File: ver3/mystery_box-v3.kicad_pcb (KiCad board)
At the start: 2 copper layers, 136 x 100 mm, 58 parts, among them J1 Screw_Terminal_01x02, J10 Screw_Terminal_01x02, J11 Screw_Terminal_01x02, J12 Screw_Terminal_01x02, J13 Screw_Terminal_01x02, J14 Screw_Terminal_01x02, J15 Screw_Terminal_01x02, J16 Screw_Terminal_01x02, J17 Screw_Terminal_01x02, J18 Barrel_Jack_MountingPin, J2 XLR3, J20 rj45-CC-X2-Aliexpress, J8 Screw_Terminal_01x02, J9 Screw_Terminal_01x02, M1 24V-Boost-Converter, Q1 IRLZ44N, Q2 IRLZ44N, Q3 IRLZ44N, U1 THVD1400D

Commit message: logo + silk stuff
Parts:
- added 12V_FAN: Conn_01x02_Pin, Connector_PinHeader_2.54mm:PinHeader_1x02_P2.54mm_Vertical, F.Cu at (259.1, 72.3)
- U3: value ~ -> smart switch
- renumbered GREEN1 to PWR_LED, switched_output_01 to SW_01, switched_output_02 to SW_02, switched_output_03 to SW_03
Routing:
- net VCC 12V: track 191.7 -> 203.5 mm
- net VCC 5V USB: track 88.4 -> 78.6 mm
- net Net-(U3-IN): track 57.9 -> 62.2 mm
- net Net-(U3-ST): track 55.8 -> 59.3 mm
- net GND: track 0.00 -> 2.87 mm, vias 1 -> 28
- net VCC 12V SW: track 356.7 -> 356.1 mm
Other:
- board text added: "+ -"
- board text added: "- d +"
- board text added: "12V always ON"
- board text added: "12V always ON fused"
- board text added: "Cosmic Cable Ltd. Mystery Box Pro"
- board text added: "RX"
- board text added: "TX"
- board text added: "rev. 1"
- board text added: "v3"

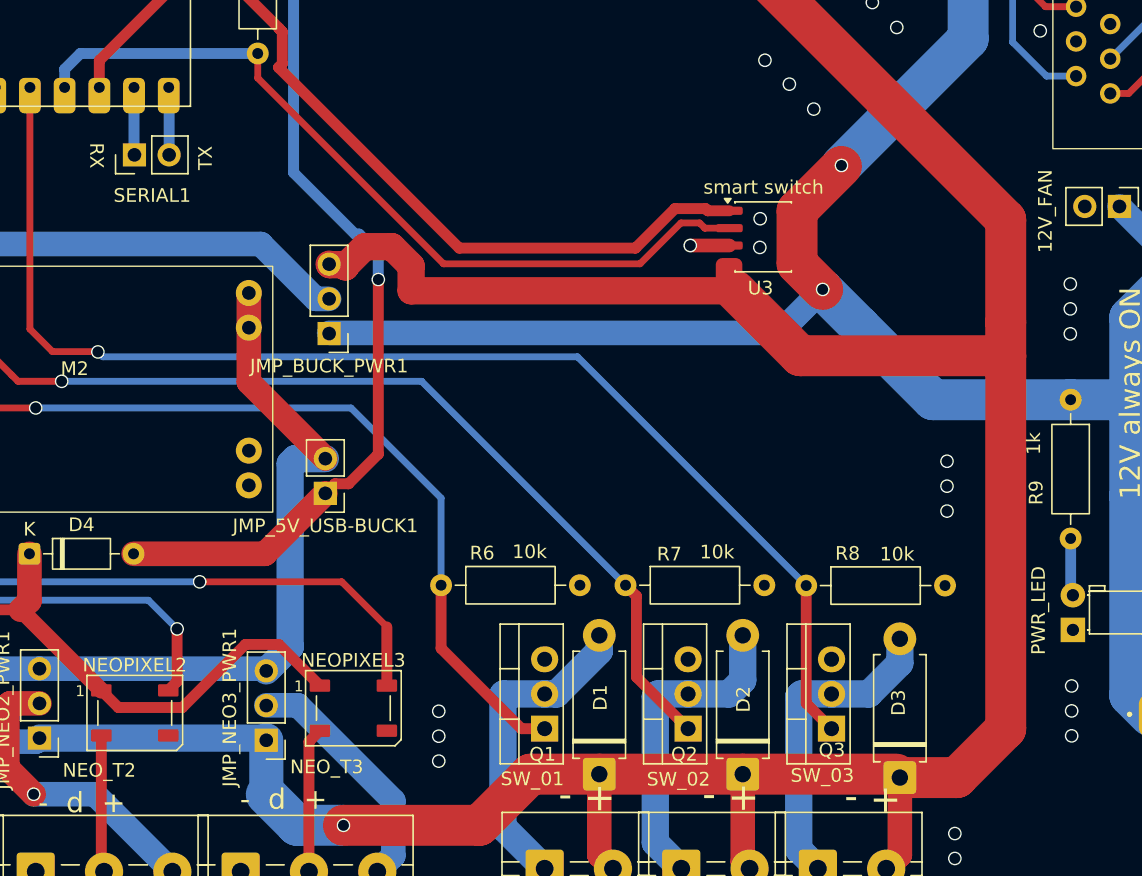
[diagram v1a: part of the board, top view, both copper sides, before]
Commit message: ver3: added GND to serial1
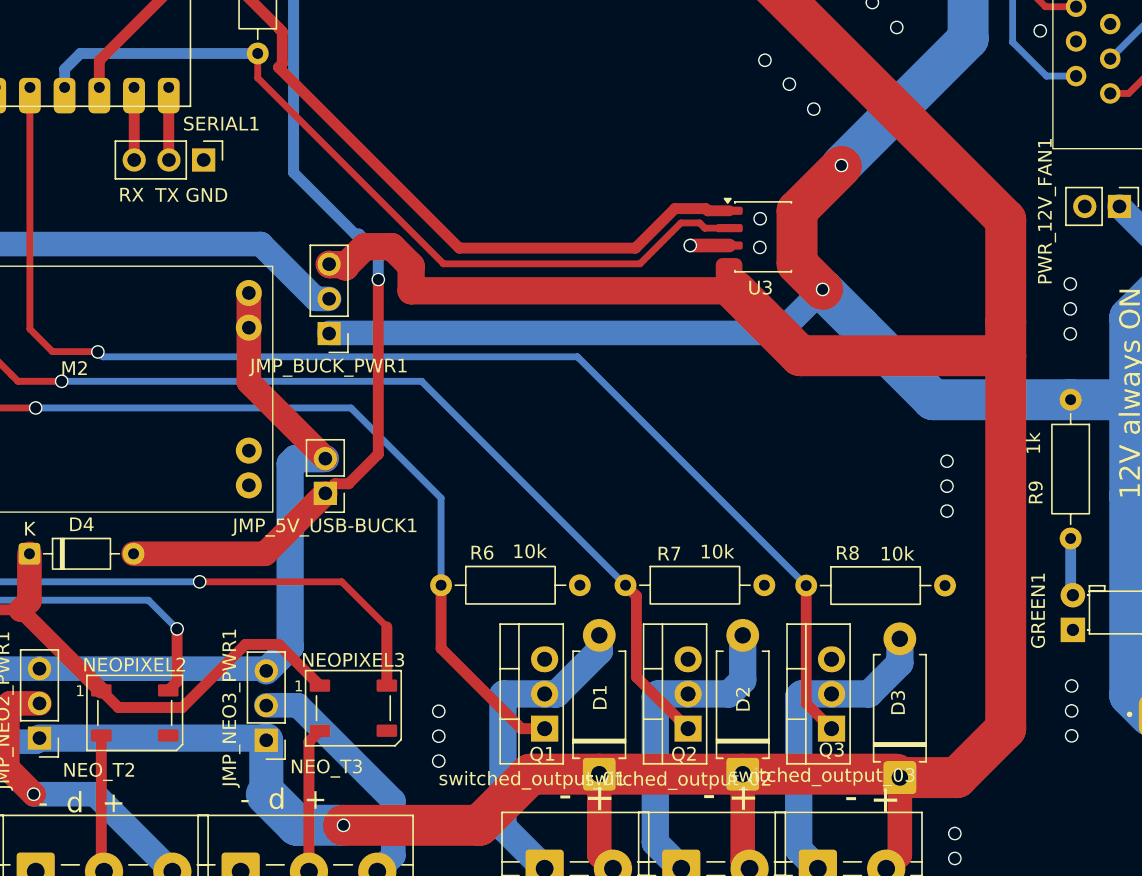
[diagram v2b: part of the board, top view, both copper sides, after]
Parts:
- removed SERIAL1: Conn_01x02_Pin, Connector_PinHeader_2.54mm:PinHeader_1x02_P2.54mm_Vertical
- added J3: SERIAL1, Connector_PinHeader_2.54mm:PinHeader_1x03_P2.54mm_Vertical, F.Cu at (192.0, 68.9)
- U3: value smart switch -> ~
- renumbered PWR_LED to GREEN1, 12V_FAN to PWR_12V_FAN1, SW_01 to switched_output_01, SW_02 to switched_output_02, SW_03 to switched_output_03
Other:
- board text added: "GND"

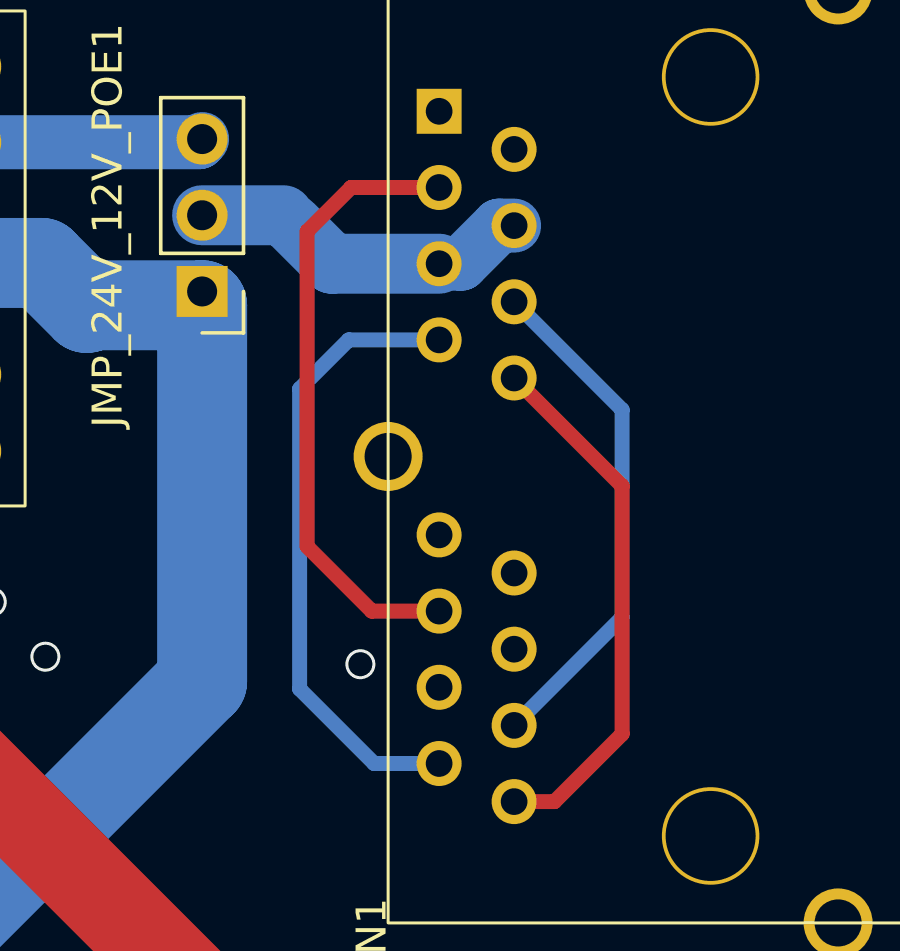
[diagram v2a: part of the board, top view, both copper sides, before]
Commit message: ver3: RJ45 data routing on same side
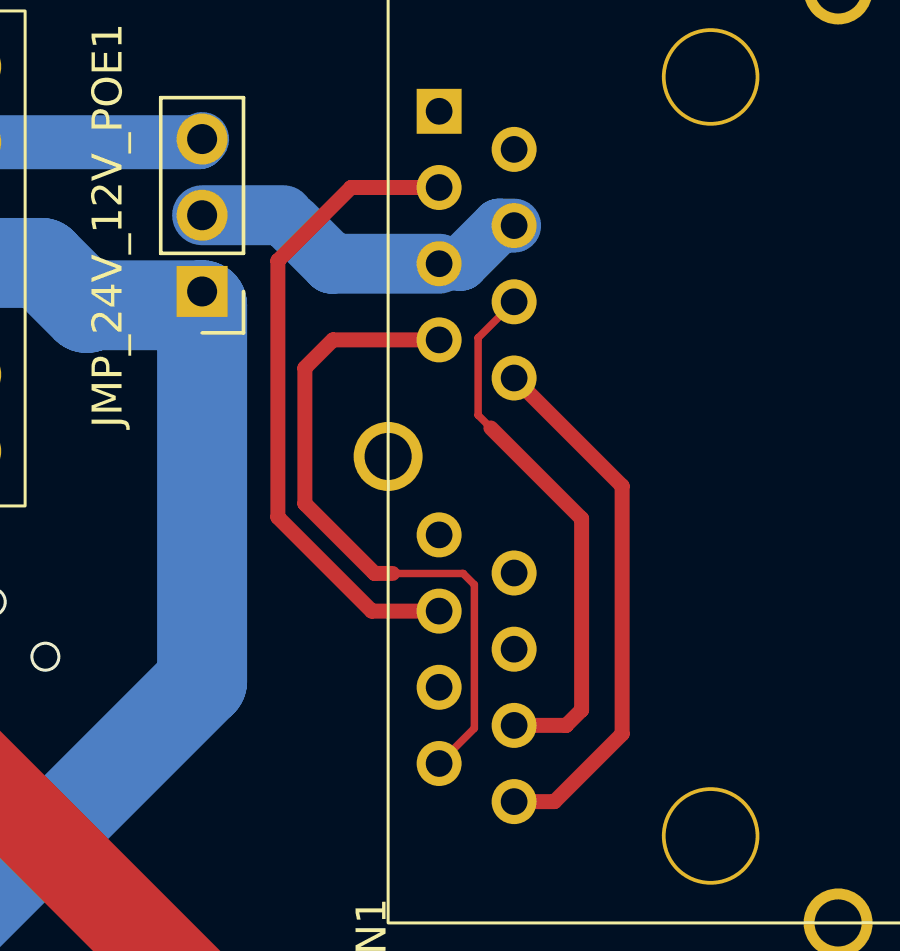
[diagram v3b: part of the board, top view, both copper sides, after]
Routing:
- net Net-(J20-Pad10): track 21.0 -> 22.6 mm
- net Net-(J20-Pad11): track 17.1 -> 18.0 mm
- net Net-(J20-Pad14): track 20.8 -> 21.6 mm
- net GND: vias 28 -> 27
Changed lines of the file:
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@@
 			(net 29 "Net-(J20-Pad14)")
 			(pintype "passive")
+			(clearance 0)
 		)
 		(pad "7" thru_hole circle
@@
 			(net 30 "unconnected-(J20-Pad7)")
 			(pintype "passive")
+			(clearance 0)
 		)
 		(pad "8" thru_hole circle
@@
 			(net 34 "unconnected-(J20-Pad8)")
 			(pintype "passive")
+			(clearance 0)
 		)
 		(pad "9" thru_hole circle
@@
 	)
 	(via
-		(at 253.275 59.425)
-		(size 1)
-		(drill 0.8)
-		(layers "F.Cu" "B.Cu")
-		(free yes)
-		(net 2)
-	)
-	(via
 		(at 247.025 121.825)
 		(size 1)
@@
 	)
 	(segment
-		(start 258.4 47.345)
-		(end 262 50.945)
+		(start 260.135 61.465)
+		(end 258.4 61.465)
 		(width 0.5)
-		(layer "B.Cu")
+		(layer "F.Cu")
 		(net 28)
 	)
 	(segment
-		(start 262 57.865)
-		(end 258.4 61.465)
+		(start 257.2 48.545)
+		(end 258.4 47.345)
+		(width 0.25)
+		(layer "F.Cu")
+		(net 28)
+	)
+	(segment
+		(start 260.65 60.95)
+		(end 260.135 61.465)
 		(width 0.5)
-		(layer "B.Cu")
+		(layer "F.Cu")
 		(net 28)
 	)
 	(segment
-		(start 262 50.945)
-		(end 262 57.865)
+		(start 257.2 51.125)
+		(end 257.2 48.545)
+		(width 0.25)
+		(layer "F.Cu")
+		(net 28)
+	)
+	(segment
+		(start 257.625 51.55)
+		(end 257.2 51.125)
+		(width 0.25)
+		(layer "F.Cu")
+		(net 28)
+	)
+	(segment
+		(start 257.625 51.55)
+		(end 260.65 54.575)
 		(width 0.5)
-		(layer "B.Cu")
+		(layer "F.Cu")
 		(net 28)
 	)
 	(segment
-		(start 251.5 45)
-		(end 251.5 55.5)
+		(start 260.65 54.575)
+		(end 260.65 60.95)
 		(width 0.5)
 		(layer "F.Cu")
-		(net 29)
+		(net 28)
 	)
 	(segment
 		(start 252.965 43.535)
-		(end 251.5 45)
+		(end 250.525 45.975)
 		(width 0.5)
 		(layer "F.Cu")
@@
 	)
 	(segment
-		(start 251.5 55.5)
-		(end 253.655 57.655)
+		(start 255.9 43.535)
+		(end 252.965 43.535)
+		(width 0.5)
+		(layer "F.Cu")
+		(net 29)
+	)
+	(segment
+		(start 250.525 45.975)
+		(end 250.525 54.525)
 		(width 0.5)
 		(layer "F.Cu")
@@
 	)
 	(segment
-		(start 255.9 43.535)
-		(end 252.965 43.535)
+		(start 250.525 54.525)
+		(end 253.655 57.655)
 		(width 0.5)
 		(layer "F.Cu")
@@
 	)
 	(segment
-		(start 252.885 48.615)
-		(end 251.25 50.25)
+		(start 251.425 54.075)
+		(end 251.425 49.55)
 		(width 0.5)
-		(layer "B.Cu")
+		(layer "F.Cu")
 		(net 32)
 	)
 	(segment
-		(start 255.9 48.615)
-		(end 252.885 48.615)
+		(start 254.35 56.4)
+		(end 256.7 56.4)
+		(width 0.25)
+		(layer "F.Cu")
+		(net 32)
+	)
+	(segment
+		(start 254.35 56.4)
+		(end 253.75 56.4)
 		(width 0.5)
-		(layer "B.Cu")
+		(layer "F.Cu")
+		(net 32)
+	)
+	(segment
+		(start 256.7 56.4)
+		(end 257.075 56.775)
+		(width 0.25)
+		(layer "F.Cu")
 		(net 32)
 	)
 	(segment
-		(start 251.25 60.25)
-		(end 253.735 62.735)
+		(start 251.425 49.55)
+		(end 252.36 48.615)
 		(width 0.5)
-		(layer "B.Cu")
+		(layer "F.Cu")
 		(net 32)
 	)
 	(segment
-		(start 251.25 50.25)
-		(end 251.25 60.25)
+		(start 253.75 56.4)
+		(end 251.425 54.075)
 		(width 0.5)
-		(layer "B.Cu")
+		(layer "F.Cu")
 		(net 32)
 	)
 	(segment
-		(start 253.735 62.735)
-		(end 255.9 62.735)
+		(start 252.36 48.615)
+		(end 255.9 48.615)
 		(width 0.5)
-		(layer "B.Cu")
+		(layer "F.Cu")
+		(net 32)
+	)
+	(segment
+		(start 257.075 61.56)
+		(end 255.9 62.735)
+		(width 0.25)
+		(layer "F.Cu")
+		(net 32)
+	)
+	(segment
+		(start 257.075 56.775)
+		(end 257.075 61.56)
+		(width 0.25)
+		(layer "F.Cu")
 		(net 32)
 	)

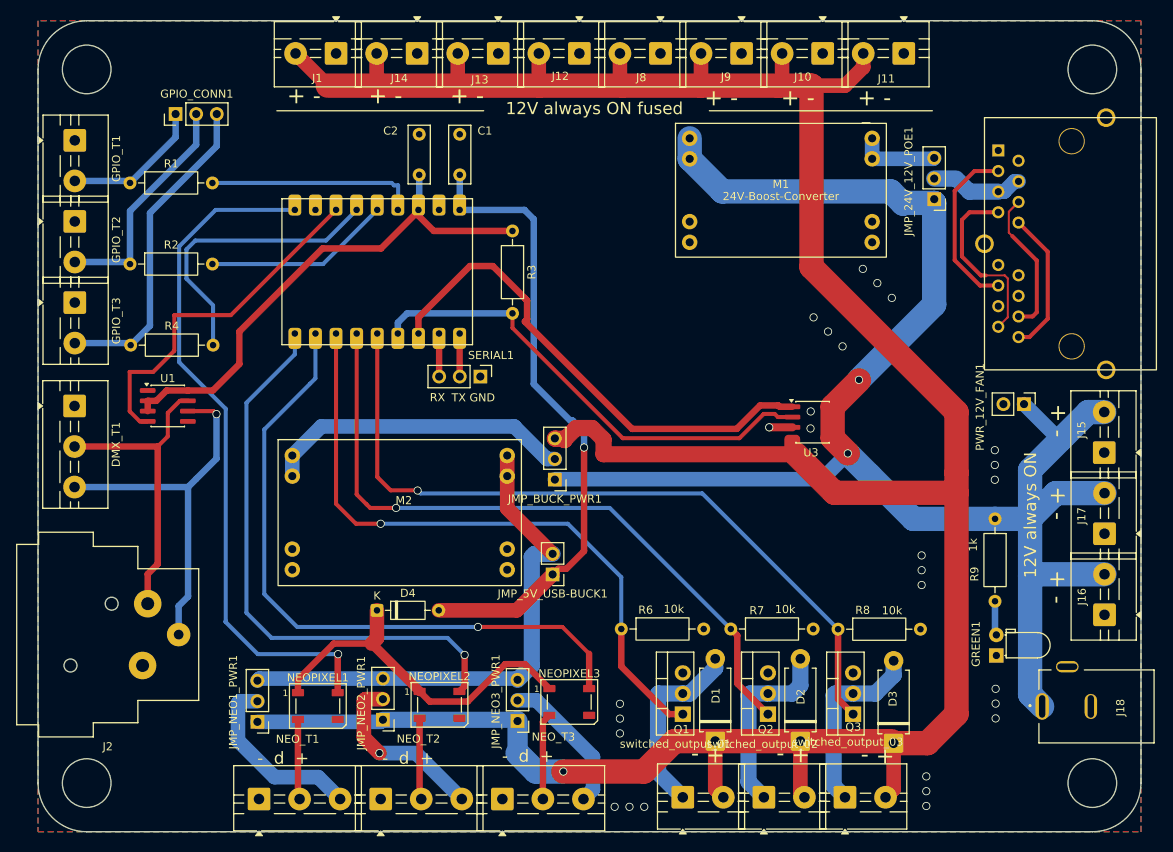
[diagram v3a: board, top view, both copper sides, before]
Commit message: ver3: silkscreen beaty & 12v fused LED
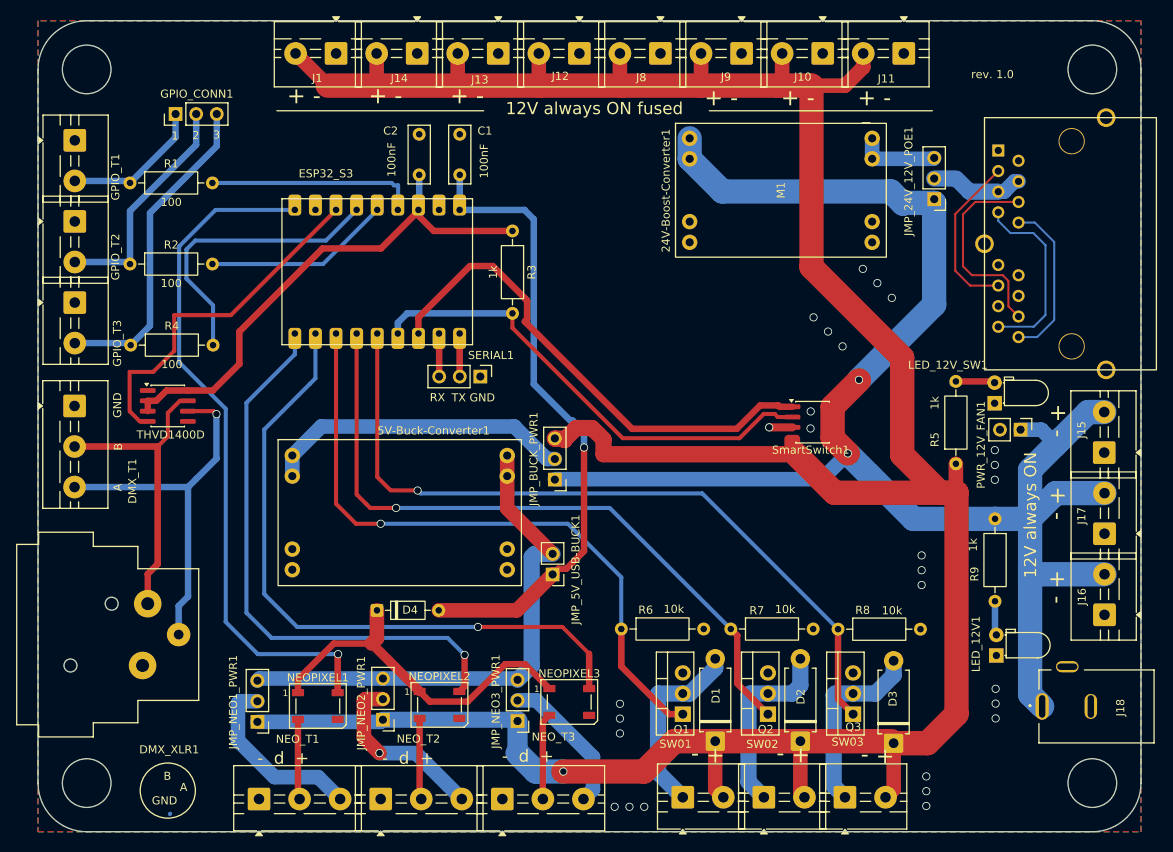
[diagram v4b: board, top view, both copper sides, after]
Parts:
- added LED_12V_SW1: LED, LED_THT:LED_D3.0mm_Horizontal_O1.27mm_Z2.0mm_Clear, F.Cu at (255.4, 72.2)
- added R5: 1k, Resistor_THT:R_Axial_DIN0207_L6.3mm_D2.5mm_P10.16mm_Horizontal, F.Cu at (250.7, 79.6)
- 24V-Boost-Converter1: renamed from M1; value 24V-Boost-Converter -> M1
- 5V-Buck-Converter1: renamed from M2; value ~ -> M2
- SmartSwitch1: renamed from U3; value ~ -> U3
- moved PWR_12V_FAN1 3.18 mm to (258.6, 75.4)
- renumbered J2 to DMX_XLR1, GREEN1 to LED_12V1, switched_output_01 to SW01, switched_output_02 to SW02, switched_output_03 to SW03
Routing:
- net Net-(J20-Pad11): track 18.0 -> 25.1 mm
- net Net-(LED_12V_SW1-A): track 0.00 -> 4.97 mm
- net VCC 12V SW: track 356.1 -> 360.8 mm
- net Net-(J20-Pad1): track 17.9 -> 20.3 mm
- net Net-(J20-Pad14): track 21.6 -> 20.5 mm
- net VCC 12V: track 203.5 -> 202.5 mm
- net Net-(J20-Pad10): track 22.6 -> 23.2 mm
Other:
- board text added: "1"
- board text added: "2"
- board text added: "3"
- board text added: "A"
- board text added: "B"
- board text added: "rev. 1.0"

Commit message: mounting holes rework
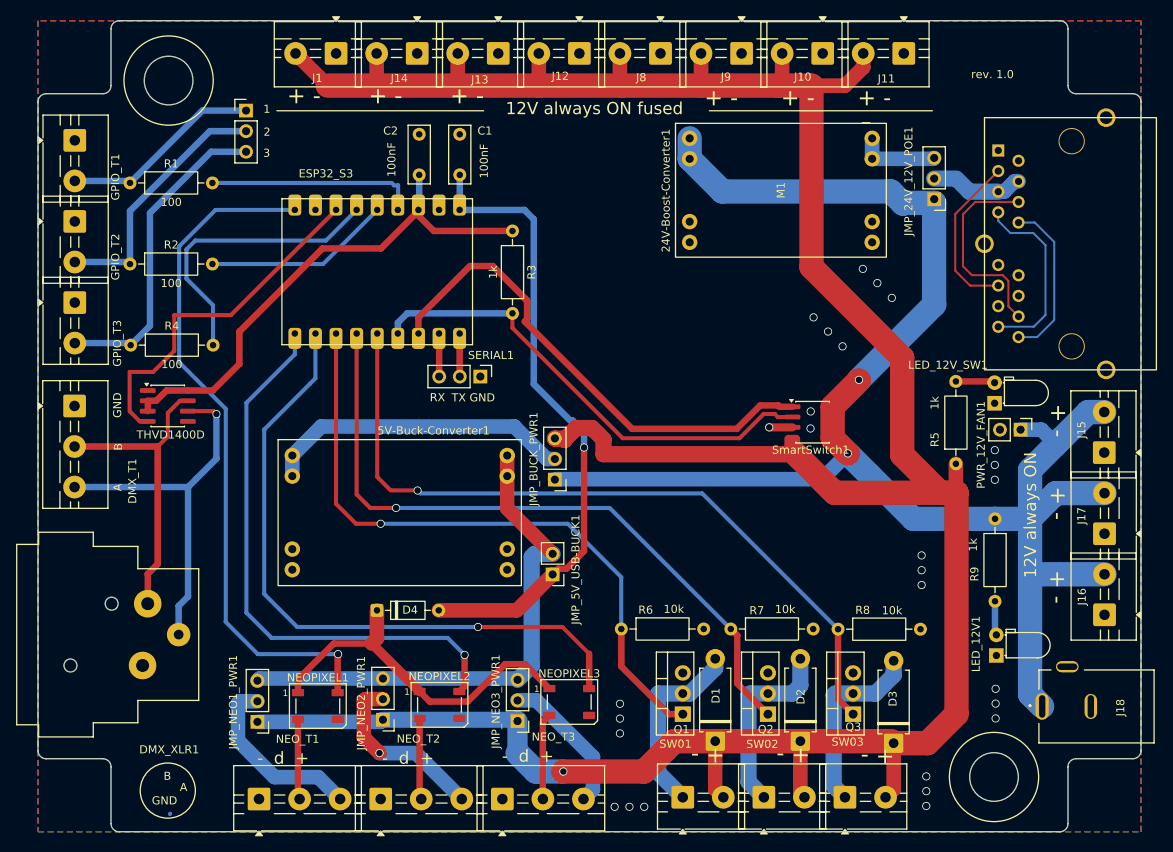
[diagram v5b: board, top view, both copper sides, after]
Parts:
- moved GPIO_CONN1 8.70 mm to (163.2, 36.1), turned to 0 degrees
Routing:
- net Net-(GPIO_CONN1-Pin_1): track 17.7 -> 24.9 mm
- net Net-(GPIO_CONN1-Pin_2): track 28.8 -> 31.8 mm
- net Net-(GPIO_CONN1-Pin_3): track 39.9 -> 39.3 mm
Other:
- outline, holes or cut-outs redrawn
